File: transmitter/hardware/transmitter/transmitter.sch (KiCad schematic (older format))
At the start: 40 parts, among them J1 SOIL, J2 SOIL, J3 USB_UART, J4 PWR, J5 SOIL, J6 SOIL, J7 SOIL, J8 SOIL, Q1 Si2305CDS, Q2 BSS138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

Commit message: Assigned footprints
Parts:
- C4: footprint (none) -> Capacitor_SMD:C_0603_1608Metric_Pad1.05x0.95mm_HandSolder
- SW1: footprint (none) -> Button_Switch_THT:SW_Tactile_Straight_KSA0Axx1LFTR
- U2: footprint (none) -> Package_TO_SOT_SMD:SOT-23-6_Handsoldering
- U4: footprint (none) -> Package_TO_SOT_SMD:SOT-223-6
- U5: footprint (none) -> Package_TO_SOT_SMD:SOT-23-5_HandSoldering
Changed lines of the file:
@@
 F 0 "U2" H 5725 2400 50  0000 C CNN
 F 1 "tpl5111" H 5450 2400 50  0000 C CNN
-F 2 "" H 5600 2700 50  0001 C CNN
+F 2 "Package_TO_SOT_SMD:SOT-23-6_Handsoldering" H 5600 2700 50  0001 C CNN
 F 3 "http://www.ti.com/lit/ds/symlink/tpl5111.pdf" H 5600 2700 50  0001 C CNN
 	1    5600 2700
@@
 F 0 "C4" H 4300 2575 50  0000 L CNN
 F 1 "0.1uF" H 4250 2475 50  0000 L CNN
-F 2 "" H 4500 2550 50  0001 C CNN
+F 2 "Capacitor_SMD:C_0603_1608Metric_Pad1.05x0.95mm_HandSolder" H 4500 2550 50  0001 C CNN
 F 3 "~" H 4500 2550 50  0001 C CNN
 	1    4500 2550
@@
 F 0 "SW1" H 5175 3200 50  0000 R CNN
 F 1 "SW_Push" H 5275 3300 50  0000 R CNN
-F 2 "" H 5100 3575 50  0001 C CNN
+F 2 "Button_Switch_THT:SW_Tactile_Straight_KSA0Axx1LFTR" H 5100 3575 50  0001 C CNN
 F 3 "" H 5100 3575 50  0001 C CNN
 	1    5100 3375
@@
 F 0 "U4" H 7625 2475 50  0000 C CNN
 F 1 "tps73733" H 7400 3025 50  0000 C CNN
-F 2 "" H 7400 2750 50  0001 C CNN
+F 2 "Package_TO_SOT_SMD:SOT-223-6" H 7400 2750 50  0001 C CNN
 F 3 "http://www.ti.com/lit/ds/symlink/tps737.pdf" H 7400 2750 50  0001 C CNN
 	1    7400 2750
@@
 F 0 "U5" H 1850 3140 50  0000 C CNN
 F 1 "BD4833G" H 1850 3049 50  0000 C CNN
-F 2 "" H 1850 3025 50  0001 C CNN
+F 2 "Package_TO_SOT_SMD:SOT-23-5_HandSoldering" H 1850 3025 50  0001 C CNN
 F 3 "http://www.farnell.com/datasheets/2293328.pdf" H 1850 3025 50  0001 C CNN
 	1    1850 3025

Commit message: Start of placement
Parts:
- SW1: footprint Button_Switch_THT:SW_Tactile_Straight_KSA0Axx1LFTR -> Button_Switch_THT:SW_Tactile_Straight_KSL0Axx1LFTR
- U2: footprint Package_TO_SOT_SMD:SOT-23-6_Handsoldering -> Package_TO_SOT_SMD:SuperSOT-6
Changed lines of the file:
@@
 F 0 "U2" H 5725 2400 50  0000 C CNN
 F 1 "tpl5111" H 5450 2400 50  0000 C CNN
-F 2 "Package_TO_SOT_SMD:SOT-23-6_Handsoldering" H 5600 2700 50  0001 C CNN
+F 2 "Package_TO_SOT_SMD:SuperSOT-6" H 5600 2700 50  0001 C CNN
 F 3 "http://www.ti.com/lit/ds/symlink/tpl5111.pdf" H 5600 2700 50  0001 C CNN
 	1    5600 2700
@@
 F 0 "SW1" H 5175 3200 50  0000 R CNN
 F 1 "SW_Push" H 5275 3300 50  0000 R CNN
-F 2 "Button_Switch_THT:SW_Tactile_Straight_KSA0Axx1LFTR" H 5100 3575 50  0001 C CNN
+F 2 "Button_Switch_THT:SW_Tactile_Straight_KSL0Axx1LFTR" H 5100 3575 50  0001 C CNN
 F 3 "" H 5100 3575 50  0001 C CNN
 	1    5100 3375

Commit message: Smaller multiplexer
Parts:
- U3: footprint Package_DIP:DIP-16_W7.62mm -> Package_SO:SOIC-16_3.9x9.9mm_P1.27mm
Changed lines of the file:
@@
 F 0 "U3" H 4675 7050 50  0000 C CNN
 F 1 "CD4051B" H 4800 6975 50  0000 C CNN
-F 2 "Package_DIP:DIP-16_W7.62mm" H 5200 5550 50  0001 L CNN
+F 2 "Package_SO:SOIC-16_3.9x9.9mm_P1.27mm" H 5200 5550 50  0001 L CNN
 F 3 "http://www.ti.com/lit/ds/symlink/cd4052b.pdf" H 5030 6400 50  0001 C CNN
 	1    5050 6300

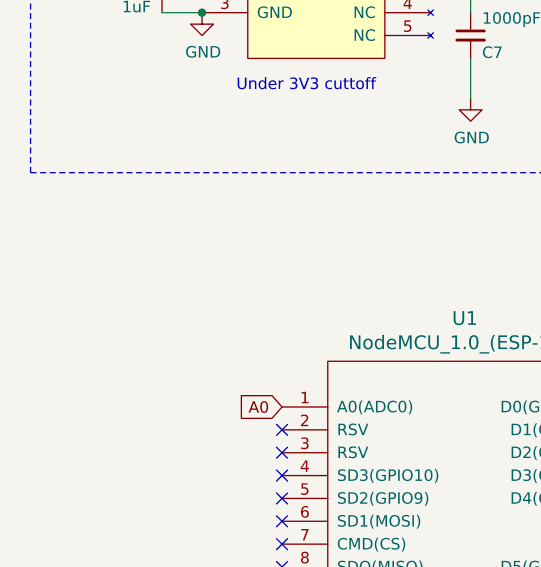
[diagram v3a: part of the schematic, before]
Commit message: Power led
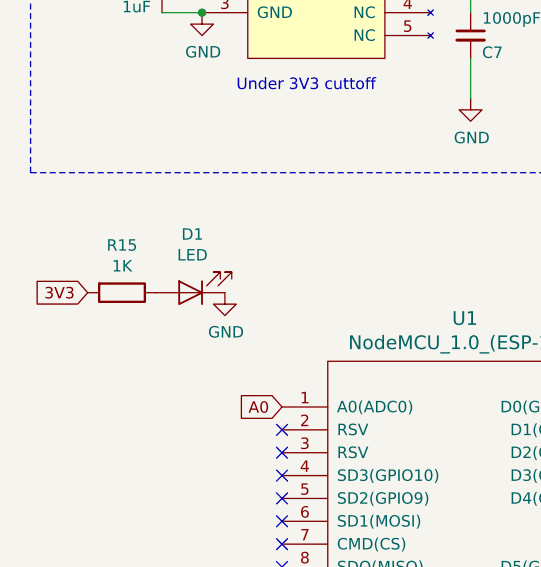
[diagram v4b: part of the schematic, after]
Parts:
- added D1: LED, LED_SMD:LED_0805_2012Metric_Pad1.15x1.40mm_HandSolder, symbol Device:LED
- added R15: 1K, Resistor_SMD:R_0603_1608Metric_Pad1.05x0.95mm_HandSolder, symbol Device:R
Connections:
- net 3V3: now also R15.2
- net GND: now also D1.1 (K)
- new net: D1.2 (A), R15.1
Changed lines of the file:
@@
 Wire Wire Line
 	5400 3375 5450 3375
+$Comp
+L Device:LED D1
+U 1 1 5E19B559
+P 1300 4600
+F 0 "D1" H 1292 4345 50  0000 C CNN
+F 1 "LED" H 1292 4436 50  0000 C CNN
+F 2 "LED_SMD:LED_0805_2012Metric_Pad1.15x1.40mm_HandSolder" H 1300 4600 50  0001 C CNN
+F 3 "~" H 1300 4600 50  0001 C CNN
+	1    1300 4600
+	-1   0    0    1
+$EndComp
+$Comp
+L power:GND #PWR024
+U 1 1 5E19B6C0
+P 1450 4600
+F 0 "#PWR024" H 1450 4350 50  0001 C CNN
+F 1 "GND" H 1455 4427 50  0000 C CNN
+F 2 "" H 1450 4600 50  0001 C CNN
+F 3 "" H 1450 4600 50  0001 C CNN
+	1    1450 4600
+	1    0    0    -1
+$EndComp
+Text GLabel 850  4600 0    50   Input ~ 0
+3V3
+$Comp
+L Device:R R15
+U 1 1 5E1AD055
+P 1000 4600
+F 0 "R15" V 793 4600 50  0000 C CNN
+F 1 "1K" V 884 4600 50  0000 C CNN
+F 2 "Resistor_SMD:R_0603_1608Metric_Pad1.05x0.95mm_HandSolder" V 930 4600 50  0001 C CNN
+F 3 "~" H 1000 4600 50  0001 C CNN
+	1    1000 4600
+	0    1    1    0
+$EndComp
 $EndSCHEMATC

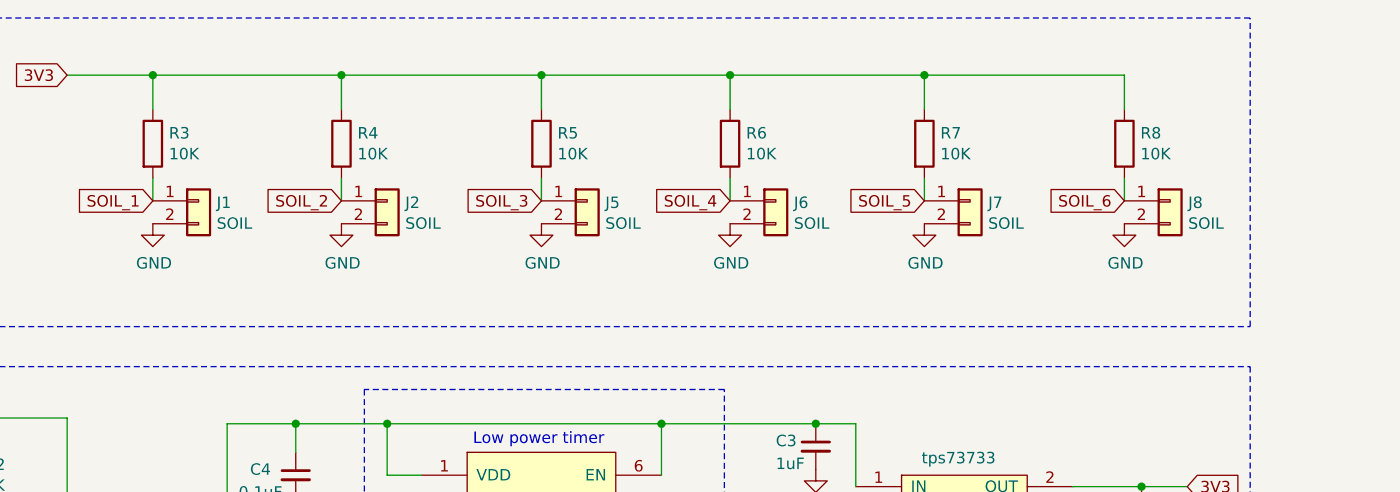
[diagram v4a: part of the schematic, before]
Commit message: Swapped sensor polarity
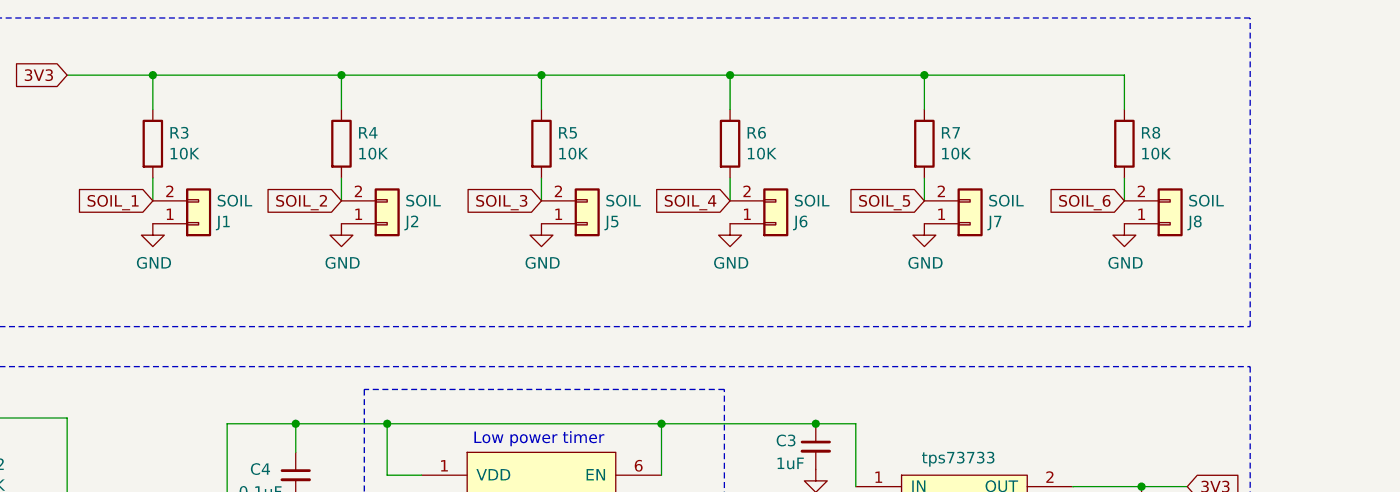
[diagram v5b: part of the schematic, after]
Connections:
- net GND: now also J1.1 (Pin_1), J2.1 (Pin_1), J5.1 (Pin_1), J6.1 (Pin_1), J7.1 (Pin_1), J8.1 (Pin_1); no longer J1.2 (Pin_2), J2.2 (Pin_2), J5.2 (Pin_2), J6.2 (Pin_2), J7.2 (Pin_2), J8.2 (Pin_2)
- net SOIL_1: now also J1.2 (Pin_2); no longer J1.1 (Pin_1)
- net SOIL_2: now also J2.2 (Pin_2); no longer J2.1 (Pin_1)
- net SOIL_3: now also J5.2 (Pin_2); no longer J5.1 (Pin_1)
- net SOIL_4: now also J6.2 (Pin_2); no longer J6.1 (Pin_1)
- net SOIL_5: now also J7.2 (Pin_2); no longer J7.1 (Pin_1)
- net SOIL_6: now also J8.2 (Pin_2); no longer J8.1 (Pin_1)
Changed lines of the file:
@@
 L Connector_Generic:Conn_01x02 J1
 U 1 1 5DBCE740
-P 4075 1350
-F 0 "J1" H 4154 1342 50  0000 L CNN
-F 1 "SOIL" H 4154 1251 50  0000 L CNN
-F 2 "Connector_JST:JST_XH_B02B-XH-A_1x02_P2.50mm_Vertical" H 4075 1350 50  0001 C CNN
-F 3 "~" H 4075 1350 50  0001 C CNN
-	1    4075 1350
-	1    0    0    -1
+P 4075 1450
+F 0 "J1" H 4154 1442 50  0000 L CNN
+F 1 "SOIL" H 4154 1351 50  0000 L CNN
+F 2 "Connector_JST:JST_XH_B02B-XH-A_1x02_P2.50mm_Vertical" H 4075 1450 50  0001 C CNN
+F 3 "~" H 4075 1450 50  0001 C CNN
+	1    4075 1450
+	1    0    0    1
 $EndComp
 Wire Wire Line
@@
 L Connector_Generic:Conn_01x02 J2
 U 1 1 5DBD7696
-P 4900 1350
-F 0 "J2" H 4979 1342 50  0000 L CNN
-F 1 "SOIL" H 4979 1251 50  0000 L CNN
-F 2 "Connector_JST:JST_XH_B02B-XH-A_1x02_P2.50mm_Vertical" H 4900 1350 50  0001 C CNN
-F 3 "~" H 4900 1350 50  0001 C CNN
-	1    4900 1350
-	1    0    0    -1
+P 4900 1450
+F 0 "J2" H 4979 1442 50  0000 L CNN
+F 1 "SOIL" H 4979 1351 50  0000 L CNN
+F 2 "Connector_JST:JST_XH_B02B-XH-A_1x02_P2.50mm_Vertical" H 4900 1450 50  0001 C CNN
+F 3 "~" H 4900 1450 50  0001 C CNN
+	1    4900 1450
+	1    0    0    1
 $EndComp
 Wire Wire Line
@@
 L Connector_Generic:Conn_01x02 J5
 U 1 1 5DBD8349
-P 5775 1350
-F 0 "J5" H 5854 1342 50  0000 L CNN
-F 1 "SOIL" H 5854 1251 50  0000 L CNN
-F 2 "Connector_JST:JST_XH_B02B-XH-A_1x02_P2.50mm_Vertical" H 5775 1350 50  0001 C CNN
-F 3 "~" H 5775 1350 50  0001 C CNN
-	1    5775 1350
-	1    0    0    -1
+P 5775 1450
+F 0 "J5" H 5854 1442 50  0000 L CNN
+F 1 "SOIL" H 5854 1351 50  0000 L CNN
+F 2 "Connector_JST:JST_XH_B02B-XH-A_1x02_P2.50mm_Vertical" H 5775 1450 50  0001 C CNN
+F 3 "~" H 5775 1450 50  0001 C CNN
+	1    5775 1450
+	1    0    0    1
 $EndComp
 Wire Wire Line
@@
 L Connector_Generic:Conn_01x02 J6
 U 1 1 5DBD8360
-P 6600 1350
-F 0 "J6" H 6679 1342 50  0000 L CNN
-F 1 "SOIL" H 6679 1251 50  0000 L CNN
-F 2 "Connector_JST:JST_XH_B02B-XH-A_1x02_P2.50mm_Vertical" H 6600 1350 50  0001 C CNN
-F 3 "~" H 6600 1350 50  0001 C CNN
-	1    6600 1350
-	1    0    0    -1
+P 6600 1450
+F 0 "J6" H 6679 1442 50  0000 L CNN
+F 1 "SOIL" H 6679 1351 50  0000 L CNN
+F 2 "Connector_JST:JST_XH_B02B-XH-A_1x02_P2.50mm_Vertical" H 6600 1450 50  0001 C CNN
+F 3 "~" H 6600 1450 50  0001 C CNN
+	1    6600 1450
+	1    0    0    1
 $EndComp
 Wire Wire Line
@@
 L Connector_Generic:Conn_01x02 J7
 U 1 1 5DBDBB99
-P 7450 1350
-F 0 "J7" H 7529 1342 50  0000 L CNN
-F 1 "SOIL" H 7529 1251 50  0000 L CNN
-F 2 "Connector_JST:JST_XH_B02B-XH-A_1x02_P2.50mm_Vertical" H 7450 1350 50  0001 C CNN
-F 3 "~" H 7450 1350 50  0001 C CNN
-	1    7450 1350
-	1    0    0    -1
+P 7450 1450
+F 0 "J7" H 7529 1442 50  0000 L CNN
+F 1 "SOIL" H 7529 1351 50  0000 L CNN
+F 2 "Connector_JST:JST_XH_B02B-XH-A_1x02_P2.50mm_Vertical" H 7450 1450 50  0001 C CNN
+F 3 "~" H 7450 1450 50  0001 C CNN
+	1    7450 1450
+	1    0    0    1
 $EndComp
 Wire Wire Line
@@
 L Connector_Generic:Conn_01x02 J8
 U 1 1 5DBDBBAF
-P 8325 1350
-F 0 "J8" H 8404 1342 50  0000 L CNN
-F 1 "SOIL" H 8404 1251 50  0000 L CNN
-F 2 "Connector_JST:JST_XH_B02B-XH-A_1x02_P2.50mm_Vertical" H 8325 1350 50  0001 C CNN
-F 3 "~" H 8325 1350 50  0001 C CNN
-	1    8325 1350
-	1    0    0    -1
+P 8325 1450
+F 0 "J8" H 8404 1442 50  0000 L CNN
+F 1 "SOIL" H 8404 1351 50  0000 L CNN
+F 2 "Connector_JST:JST_XH_B02B-XH-A_1x02_P2.50mm_Vertical" H 8325 1450 50  0001 C CNN
+F 3 "~" H 8325 1450 50  0001 C CNN
+	1    8325 1450
+	1    0    0    1
 $EndComp
 Wire Wire Line

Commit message: Measure the delay time
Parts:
- added JP1: Jumper, Jumper:SolderJumper-2_P1.3mm_Open_RoundedPad1.0x1.5mm, symbol Device:Jumper_NO_Small
- added R16, R19: 10K, Resistor_SMD:R_0603_1608Metric_Pad1.05x0.95mm_HandSolder, symbol Device:R
- added R18: 100K, Resistor_SMD:R_0603_1608Metric_Pad1.05x0.95mm_HandSolder, symbol Device:R
- added TP1: TestPoint, TestPoint:TestPoint_Pad_D1.0mm, symbol Connector:TestPoint
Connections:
- net GND: now also R19.1
- net at U1.28 (D2(GPIO4)): now also R16.2
- net DELAY_VAL: now reaches U3.4 (X7)
- net DELAY_VAL: now also JP1.1, R16.1, R18.2
- net at U2.5 (DRIVn), U4.5 (EN): now also TP1.1
- net at R13.2, SW1.2, U2.3 (DELAY): now also JP1.2
- new net: R18.1, R19.2
- no-connect marks 19 -> 17
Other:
- note added: "Copy of the \ntpl511 resistors\nso the payload can \nsend the delay time.\n(don't populate \nif jumpered to SW1)"
- moved on the sheet: D1, R15
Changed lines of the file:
@@
 Wire Wire Line
 	5325 4950 5325 4975
-NoConn ~ 3300 5300
 NoConn ~ 3300 5400
 NoConn ~ 3300 5500
@@
 Text GLabel 5550 6700 2    50   Input ~ 0
 SOIL_6
-NoConn ~ 5550 6800
 Text Label 1500 6500 0    50   ~ 0
 VBAT
@@
 	6100 2700 6325 2700
 Wire Wire Line
-	6325 2900 6950 2900
+	6325 2900 6575 2900
 NoConn ~ 7900 2900
-NoConn ~ 3300 5100
 Text GLabel 5100 4700 0    50   Input ~ 0
 3V3
-NoConn ~ 1700 6300
 Wire Wire Line
 	3300 5800 4550 5800
@@
 L Device:LED D1
 U 1 1 5E19B559
-P 1300 4600
-F 0 "D1" H 1292 4345 50  0000 C CNN
-F 1 "LED" H 1292 4436 50  0000 C CNN
-F 2 "LED_SMD:LED_0805_2012Metric_Pad1.15x1.40mm_HandSolder" H 1300 4600 50  0001 C CNN
-F 3 "~" H 1300 4600 50  0001 C CNN
-	1    1300 4600
+P 2675 7325
+F 0 "D1" H 2667 7070 50  0000 C CNN
+F 1 "LED" H 2667 7161 50  0000 C CNN
+F 2 "LED_SMD:LED_0805_2012Metric_Pad1.15x1.40mm_HandSolder" H 2675 7325 50  0001 C CNN
+F 3 "~" H 2675 7325 50  0001 C CNN
+	1    2675 7325
 	-1   0    0    1
 $EndComp
@@
 L power:GND #PWR024
 U 1 1 5E19B6C0
-P 1450 4600
-F 0 "#PWR024" H 1450 4350 50  0001 C CNN
-F 1 "GND" H 1455 4427 50  0000 C CNN
-F 2 "" H 1450 4600 50  0001 C CNN
-F 3 "" H 1450 4600 50  0001 C CNN
-	1    1450 4600
+P 2825 7325
+F 0 "#PWR024" H 2825 7075 50  0001 C CNN
+F 1 "GND" H 2830 7152 50  0000 C CNN
+F 2 "" H 2825 7325 50  0001 C CNN
+F 3 "" H 2825 7325 50  0001 C CNN
+	1    2825 7325
 	1    0    0    -1
 $EndComp
-Text GLabel 850  4600 0    50   Input ~ 0
+Text GLabel 2225 7325 0    50   Input ~ 0
 3V3
 $Comp
 L Device:R R15
 U 1 1 5E1AD055
-P 1000 4600
-F 0 "R15" V 793 4600 50  0000 C CNN
-F 1 "1K" V 884 4600 50  0000 C CNN
-F 2 "Resistor_SMD:R_0603_1608Metric_Pad1.05x0.95mm_HandSolder" V 930 4600 50  0001 C CNN
-F 3 "~" H 1000 4600 50  0001 C CNN
-	1    1000 4600
+P 2375 7325
+F 0 "R15" V 2168 7325 50  0000 C CNN
+F 1 "1K" V 2259 7325 50  0000 C CNN
+F 2 "Resistor_SMD:R_0603_1608Metric_Pad1.05x0.95mm_HandSolder" V 2305 7325 50  0001 C CNN
+F 3 "~" H 2375 7325 50  0001 C CNN
+	1    2375 7325
+	0    1    1    0
+$EndComp
+$Comp
+L Device:R R18
+U 1 1 5E2244F7
+P 5925 4300
+F 0 "R18" V 5850 4250 50  0000 L CNN
+F 1 "100K" V 6025 4225 50  0000 L CNN
+F 2 "Resistor_SMD:R_0603_1608Metric_Pad1.05x0.95mm_HandSolder" V 5855 4300 50  0001 C CNN
+F 3 "~" H 5925 4300 50  0001 C CNN
+	1    5925 4300
+	0    1    1    0
+$EndComp
+$Comp
+L Device:R R19
+U 1 1 5E2244FE
+P 6225 4300
+F 0 "R19" V 6150 4250 50  0000 L CNN
+F 1 "10K" V 6325 4225 50  0000 L CNN
+F 2 "Resistor_SMD:R_0603_1608Metric_Pad1.05x0.95mm_HandSolder" V 6155 4300 50  0001 C CNN
+F 3 "~" H 6225 4300 50  0001 C CNN
+	1    6225 4300
+	0    1    1    0
+$EndComp
+$Comp
+L power:GND #PWR025
+U 1 1 5E224505
+P 6500 4300
+F 0 "#PWR025" H 6500 4050 50  0001 C CNN
+F 1 "GND" H 6505 4127 50  0000 C CNN
+F 2 "" H 6500 4300 50  0001 C CNN
+F 3 "" H 6500 4300 50  0001 C CNN
+	1    6500 4300
+	1    0    0    -1
+$EndComp
+Wire Wire Line
+	6375 4300 6500 4300
+$Comp
+L Device:R R16
+U 1 1 5E227A5D
+P 5050 4300
+F 0 "R16" V 4975 4225 50  0000 L CNN
+F 1 "10K" V 5150 4225 50  0000 L CNN
+F 2 "Resistor_SMD:R_0603_1608Metric_Pad1.05x0.95mm_HandSolder" V 4980 4300 50  0001 C CNN
+F 3 "~" H 5050 4300 50  0001 C CNN
+	1    5050 4300
 	0    1    1    0
 $EndComp
+Wire Wire Line
+	3300 5300 4150 5300
+Wire Wire Line
+	5550 6800 6350 6800
+Wire Wire Line
+	6350 6800 6350 5100
+Text Notes 5900 4975 0    50   ~ 0
+Copy of the \ntpl511 resistors\nso the payload can \nsend the delay time.\n(don't populate \nif jumpered to SW1)
+NoConn ~ 1700 6300
+NoConn ~ 3300 5100
+$Comp
+L Device:Jumper_NO_Small JP1
+U 1 1 5E23713E
+P 5400 4200
+F 0 "JP1" V 5446 4152 50  0000 R CNN
+F 1 "Jumper" V 5355 4152 50  0000 R CNN
+F 2 "Jumper:SolderJumper-2_P1.3mm_Open_RoundedPad1.0x1.5mm" H 5400 4200 50  0001 C CNN
+F 3 "~" H 5400 4200 50  0001 C CNN
+	1    5400 4200
+	0    -1   -1   0
+$EndComp
+Wire Wire Line
+	5200 4300 5400 4300
+Wire Wire Line
+	5775 4300 5400 4300
+Connection ~ 5400 4300
+Wire Wire Line
+	5400 4100 5400 3375
+Wire Wire Line
+	5400 4650 5750 4650
+Wire Wire Line
+	5750 4650 5750 5100
+Wire Wire Line
+	5750 5100 6350 5100
+Wire Wire Line
+	4150 5300 4150 4300
+Wire Wire Line
+	4150 4300 4900 4300
+Wire Wire Line
+	5400 4300 5400 4650
+Text Label 5925 6800 0    50   ~ 0
+DELAY_VAL
+$Comp
+L Connector:TestPoint TP1
+U 1 1 5E26FDC7
+P 6575 2900
+F 0 "TP1" H 6500 3125 50  0000 R CNN
+F 1 "TestPoint" H 6517 3018 50  0000 R CNN
+F 2 "TestPoint:TestPoint_Pad_D1.0mm" H 6775 2900 50  0001 C CNN
+F 3 "~" H 6775 2900 50  0001 C CNN
+	1    6575 2900
+	-1   0    0    1
+$EndComp
+Connection ~ 6575 2900
+Wire Wire Line
+	6575 2900 6950 2900
 $EndSCHEMATC
